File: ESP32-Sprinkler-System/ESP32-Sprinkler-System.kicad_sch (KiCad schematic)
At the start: 18 parts, among them U101 ESP32-WROOM-32E_(16MB), U102 CH340C

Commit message: Change of plans
We had a change of plans. Rather than having everything made of surface-mount parts, we opted for a simpler through-hole project that could be breadboarded first. This circuit will be revisited and updated when the prototype is complete.
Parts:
- removed J101: (no value), symbol Connector_Generic:Conn_01x06
- removed U101: ESP32-WROOM-32E_(16MB), ESP32-WROOM-32E__16MB_:XCVR_ESP32-WROOM-32E_(16MB), symbol ESP32-WROOM-32E__16MB_:ESP32-WROOM-32E_(16MB)
- removed U102: CH340C, CH340C:SOIC127P600X180-16N, symbol CH340C:CH340C
- added J?: Soil_Moist1, symbol Connector_Generic:Conn_01x03
- added J? (x2): OLED, symbol Connector_Generic:Conn_01x04
- added J? (x4): Conn_01x19, symbol Connector_Generic:Conn_01x19
- added J?: Soil_Moist2, symbol Connector_Generic:Conn_01x03
- added J?: SoilMoist1, symbol Connector_Generic:Conn_01x03
- added J? (x2): DHT, symbol Connector_Generic:Conn_01x04
- added J? (x2): TEMP&HUMIDITY, symbol Connector_Generic:Conn_01x05
- added J?: SoilMoist2, symbol Connector_Generic:Conn_01x03
- added SW?: B, Breadstick Footprints:GT-TC029B-H025-L1N, symbol Switch:SW_Push
- added SW?: A, Breadstick Footprints:GT-TC029B-H025-L1N, symbol Switch:SW_Push
- C102: value (none) -> 1uF; footprint (none) -> Breadstick Footprints:Perfect_0402_Cap
- SW101: value (none) -> ~{RESET}
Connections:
- net +3V3: now also J?.1 (Pin_1), J?.1 (Pin_1), J?.2 (Pin_2), J?.2 (Pin_2), J?.2 (Pin_2), J?.2 (Pin_2)
- net GND: now also J?.1 (Pin_1), J?.1 (Pin_1), J?.1 (Pin_1), J?.1 (Pin_1), J?.1 (Pin_1), J?.1 (Pin_1), J?.14 (Pin_14), J?.14 (Pin_14), J?.3 (Pin_3), J?.3 (Pin_3), J?.4 (Pin_4), J?.4 (Pin_4), J?.4 (Pin_4), J?.4 (Pin_4), J?.7 (Pin_7), J?.7 (Pin_7), SW?.1, SW?.1
- new net: J?.15 (Pin_15), J?.2 (Pin_2)
- new net: J?.3 (Pin_3), J?.5 (Pin_5)
- new net: J?.3 (Pin_3), J?.6 (Pin_6)
- new net +5V: J?.1 (Pin_1), J?.1 (Pin_1), J?.1 (Pin_1), J?.1 (Pin_1), J?.19 (Pin_19), J?.19 (Pin_19), J?.3 (Pin_3), J?.3 (Pin_3)
- new net DHT: J?.15 (Pin_15), J?.2 (Pin_2)
- new net ENABLE: J?.2 (Pin_2)
- new net GPIO0: J?.14 (Pin_14), SW?.2
- new net GPIO1: J?.4 (Pin_4)
- new net GPIO10: J?.17 (Pin_17)
- new net GPIO11: J?.18 (Pin_18)
- new net GPIO12: J?.13 (Pin_13)
- new net GPIO14: J?.12 (Pin_12)
- new net GPIO15: J?.16 (Pin_16)
- new net GPIO16: J?.12 (Pin_12)
- new net GPIO17: J?.11 (Pin_11)
- new net GPIO18: J?.9 (Pin_9)
- new net GPIO19: J?.8 (Pin_8)
- new net GPIO2: J?.15 (Pin_15)
- new net GPIO21: J?.1 (Pin_1), J?.1 (Pin_1), J?.5 (Pin_5), J?.5 (Pin_5), J?.6 (Pin_6), J?.6 (Pin_6)
- new net GPIO22: J?.2 (Pin_2), J?.2 (Pin_2), J?.3 (Pin_3), J?.3 (Pin_3), J?.4 (Pin_4), J?.4 (Pin_4)
- new net GPIO23: J?.2 (Pin_2)
- new net GPIO25: J?.9 (Pin_9), J?.9 (Pin_9)
- new net GPIO26: J?.10 (Pin_10), J?.10 (Pin_10)
- new net GPIO27: J?.11 (Pin_11), J?.11 (Pin_11)
- new net GPIO3: J?.5 (Pin_5)
- new net GPIO32: J?.7 (Pin_7), J?.7 (Pin_7)
- new net GPIO33: J?.8 (Pin_8), J?.8 (Pin_8)
- new net GPIO34: J?.3 (Pin_3), J?.5 (Pin_5)
- new net GPIO35: J?.6 (Pin_6)
- new net GPIO36: J?.3 (Pin_3)
- new net GPIO39: J?.3 (Pin_3), J?.4 (Pin_4)
- new net GPIO4: J?.13 (Pin_13), SW?.2
- new net GPIO5: J?.10 (Pin_10)
- new net GPIO6: J?.19 (Pin_19)
- new net GPIO7: J?.18 (Pin_18)
- new net GPIO8: J?.17 (Pin_17)
- new net GPIO9: J?.16 (Pin_16)
- new net SWA: J?.13 (Pin_13)
- new net SWB: J?.14 (Pin_14)
- no-connect marks 0 -> 4
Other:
- note removed: "JTAG"
- note removed: "UART"
- moved on the sheet: C102, C103, C104, C105, R104, R105, SW101

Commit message: Major Update to New Through-Hole Components
Circuit has been modified to match the breadboard prototype Cody built.
Solenoid driver side is done.
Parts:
- removed C101: 30pF, Breadstick Footprints:Perfect_0402_Cap, symbol Device:C_Small
- removed C102: 1uF, Breadstick Footprints:Perfect_0402_Cap, symbol Device:C_Small
- removed C103, C104: 10uF, Breadstick Footprints:Perfect_0402_Cap, symbol Device:C_Small
- removed C105: 100uF, Capacitor_SMD:C_1206_3216Metric, symbol Device:C_Small
- removed D101: ESD_TVS, Breadstick Footprints:Perfect_0402_Resistor, symbol Device:D_TVS_Filled
- removed D102: LED_Filled, LED_SMD:LED_0805_2012Metric, symbol Device:LED_Filled
- removed D103, D104: SHOTTKY, Diode_SMD:D_SOD-123, symbol SparkFun-DiscreteSemi:DIODE-SHOTTKY_MBRA140
- removed J?: OLED, symbol Connector_Generic:Conn_01x04
- removed J? (x2): Conn_01x19, symbol Connector_Generic:Conn_01x19
- removed J?: SoilMoist1, symbol Connector_Generic:Conn_01x03
- removed J?: DHT, symbol Connector_Generic:Conn_01x04
- removed J?: SoilMoist2, symbol Connector_Generic:Conn_01x03
- removed J?: TEMP&HUMIDITY, symbol Connector_Generic:Conn_01x05
- removed R101, R102, R104: 10k, Breadstick Footprints:Perfect_0402_Resistor, symbol Device:R
- removed R103: 1k, Breadstick Footprints:Perfect_0402_Resistor, symbol Device:R
- removed R105: 27, Breadstick Footprints:Perfect_0402_Resistor, symbol Device:R
- removed SW101: ~{RESET}, Breadstick Footprints:GT-TC029B-H025-L1N, symbol Switch:SW_Push
- removed SW?: B, Breadstick Footprints:GT-TC029B-H025-L1N, symbol Switch:SW_Push
- removed SW?: A, Breadstick Footprints:GT-TC029B-H025-L1N, symbol Switch:SW_Push
- added J101: 12V, Breadstick Footprints:KF202-50-2P, symbol Connector:Screw_Terminal_01x02
- added S101: (no value), symbol SparkFun-Switches:MOMENTARY-SWITCH-SPST-2-SMD-4.6X2.8MM
- gave numbers to parts that had none: 7
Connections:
- net GND: now also J101.2 (Pin_2), S101.4
- net GPIO4: now also S101.1
- net +3V3 renamed 3.3V
- net +5V renamed 5V
- new net 12V: J101.1 (Pin_1)
- no-connect marks 4 -> 2
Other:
- removed sheet BuckConverter

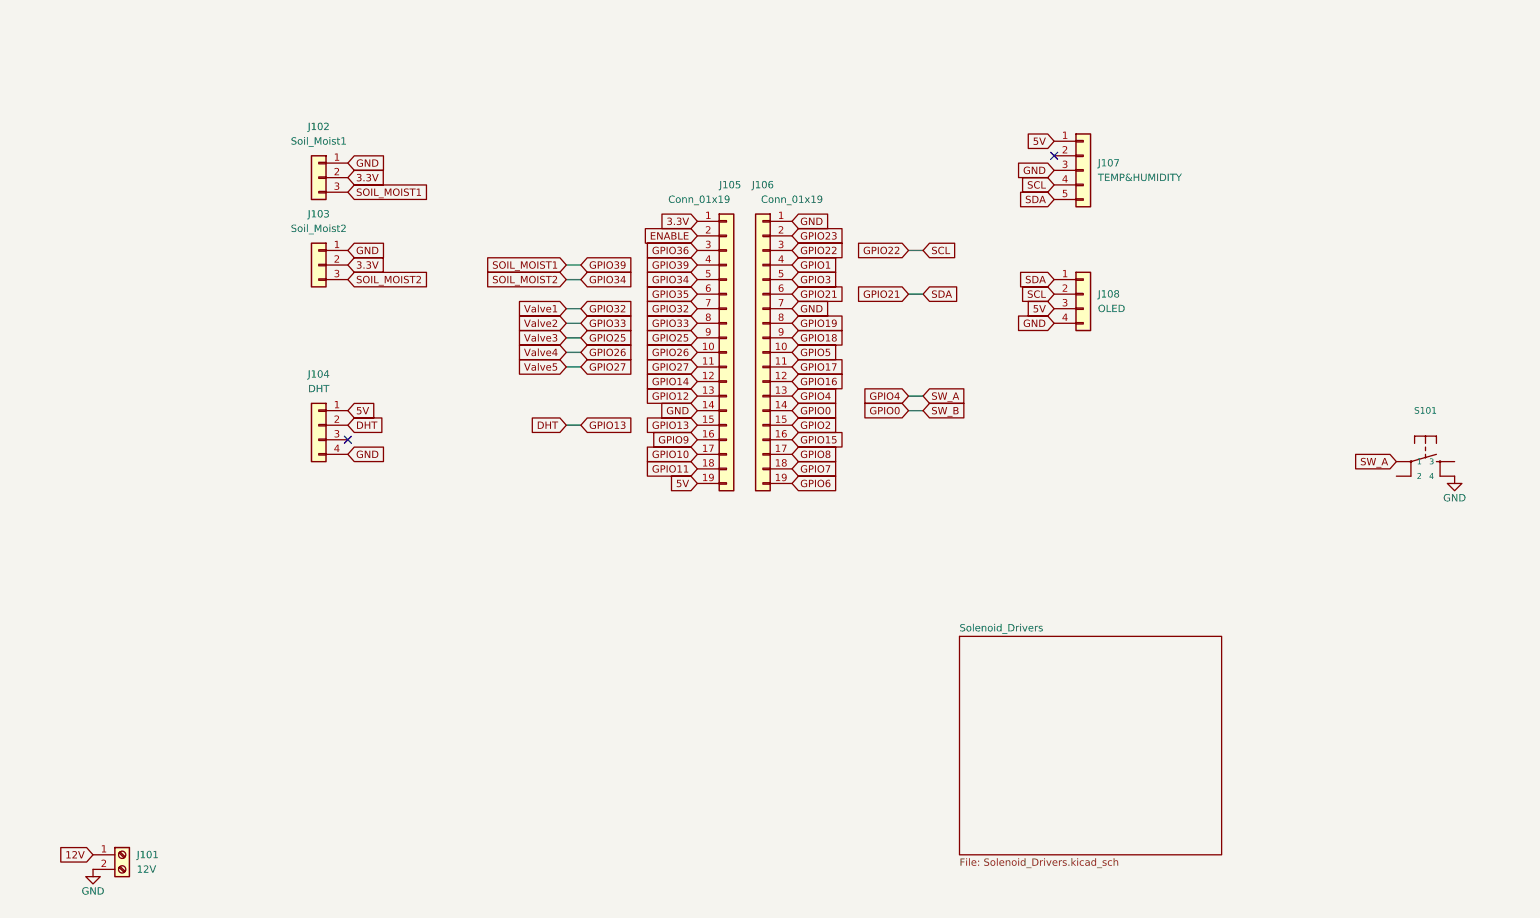
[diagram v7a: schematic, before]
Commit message: Found symbol and footprint for ESP32 DevKit, schematic 80% done.
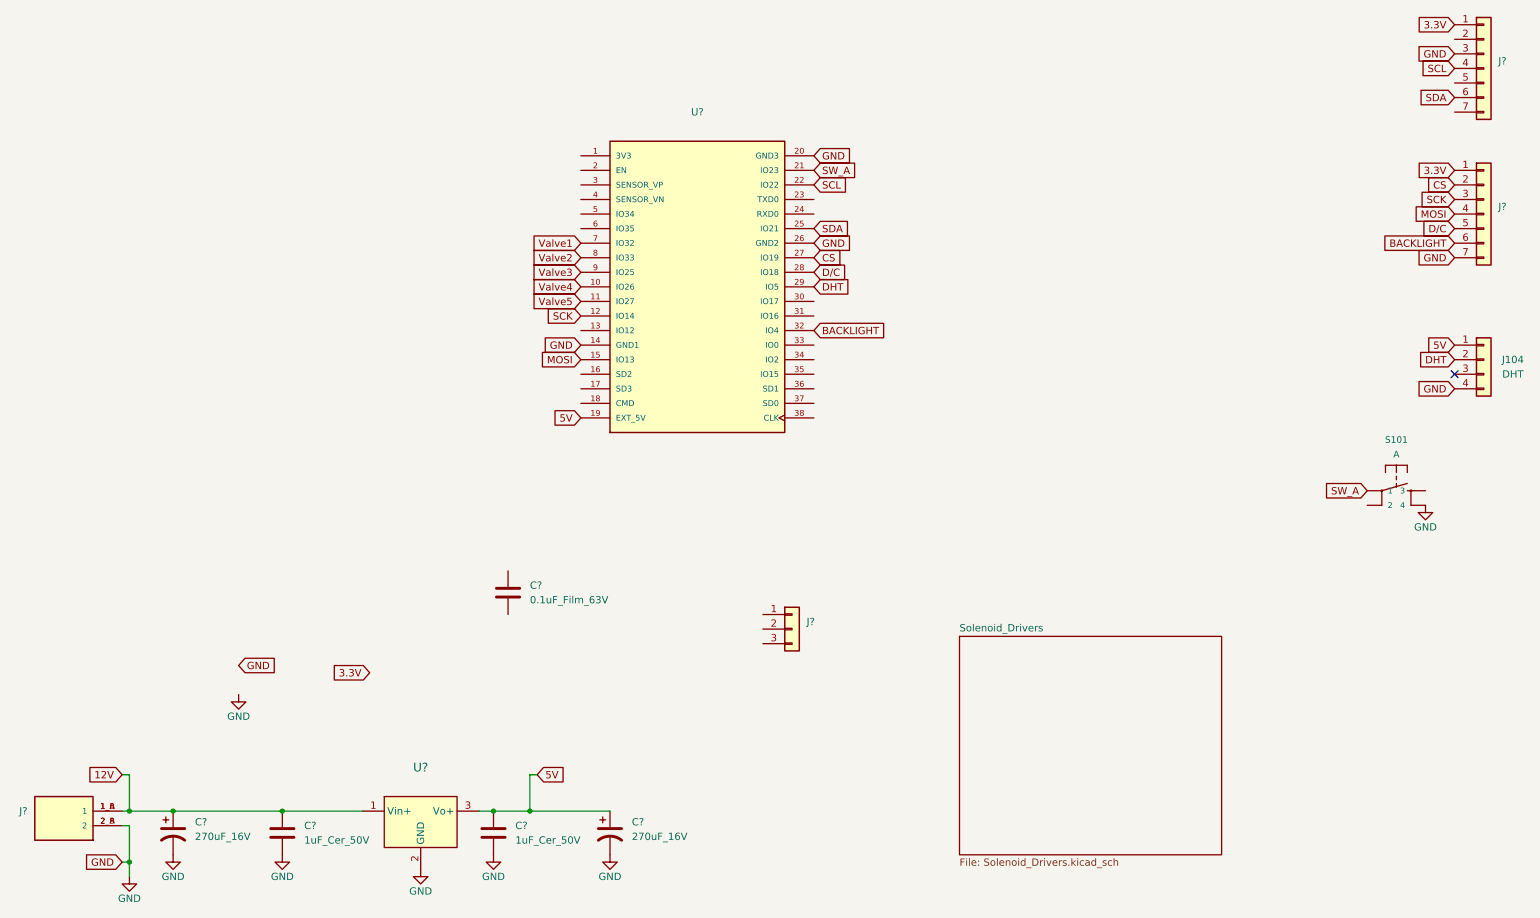
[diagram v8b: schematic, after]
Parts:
- removed J101: 12V, Breadstick Footprints:KF202-50-2P, symbol Connector:Screw_Terminal_01x02
- removed J102: Soil_Moist1, symbol Connector_Generic:Conn_01x03
- removed J103: Soil_Moist2, symbol Connector_Generic:Conn_01x03
- removed J105, J106: Conn_01x19, symbol Connector_Generic:Conn_01x19
- removed J107: TEMP&HUMIDITY, symbol Connector_Generic:Conn_01x05
- removed J108: OLED, symbol Connector_Generic:Conn_01x04
- added C? (x2): 270uF_16V, Capacitor_THT:CP_Radial_D6.3mm_P2.50mm, symbol Device:C_Polarized_US
- added C? (x2): 1uF_Cer_50V, Capacitor_THT:C_Disc_D7.5mm_W4.4mm_P5.00mm, symbol Device:C
- added C?: 0.1uF_Film_63V, Capacitor_THT:C_Rect_L7.0mm_W2.5mm_P5.00mm, symbol Device:C
- added J? (x2): (no value), symbol Connector_Generic:Conn_01x07
- added J?: (no value), symbol Connector_Generic:Conn_01x03
- added J?: (no value), TBL004-508-02BE-2GY:CUI_TBL004-508-02BE-2GY, symbol TBL004-508-02BE-2GY:TBL004-508-02BE-2GY
- added U?: (no value), symbol ESP32-DEVKITC-32D:ESP32-DEVKITC-32D
- added U?: (no value), symbol dk_DC-DC-Converters:V7805-500
- S101: value (none) -> A; footprint (none) -> Switches:TACTILE_SWITCH_PTH_12MM
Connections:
- net 12V: now also C?.1, C?.1, J?.1_A (1), J?.1_B (1), U?.1 (Vin+)
- net 3.3V: now also J?.1 (Pin_1), J?.1 (Pin_1)
- net 5V: now also C?.1, C?.1, U?.19 (EXT_5V), U?.3 (Vo+)
- net DHT: now also U?.29 (IO5)
- net GND: now also C?.2, C?.2, C?.2, C?.2, J?.2_A (2), J?.2_B (2), J?.3 (Pin_3), J?.7 (Pin_7), U?.14 (GND1), U?.2 (GND), U?.20 (GND3), U?.26 (GND2)
- net GPIO4 renamed SW_A
- net SW_A: now also U?.21 (IO23)
- new net BACKLIGHT: J?.6 (Pin_6), U?.32 (IO4)
- new net CS: J?.2 (Pin_2), U?.27 (IO19)
- new net D/C: J?.5 (Pin_5), U?.28 (IO18)
- new net MOSI: J?.4 (Pin_4), U?.15 (IO13)
- new net SCK: J?.3 (Pin_3), U?.12 (IO14)
- new net SCL: J?.4 (Pin_4), U?.22 (IO22)
- new net SDA: J?.6 (Pin_6), U?.25 (IO21)
- new net Valve1: U?.7 (IO32)
- new net Valve2: U?.8 (IO33)
- new net Valve3: U?.9 (IO25)
- new net Valve4: U?.10 (IO26)
- new net Valve5: U?.11 (IO27)
- no-connect marks 2 -> 1
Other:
- moved on the sheet: J104, S101
